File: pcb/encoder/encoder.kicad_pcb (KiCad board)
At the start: 2 copper layers, 23.7 x 15.3 mm, 18 parts, among them J1 Conn_01x05, Q1 B19H1PT, Q2 B19H1PT, Q3 B19H1PT, Q4 B19H1PT, U1 LM358LV

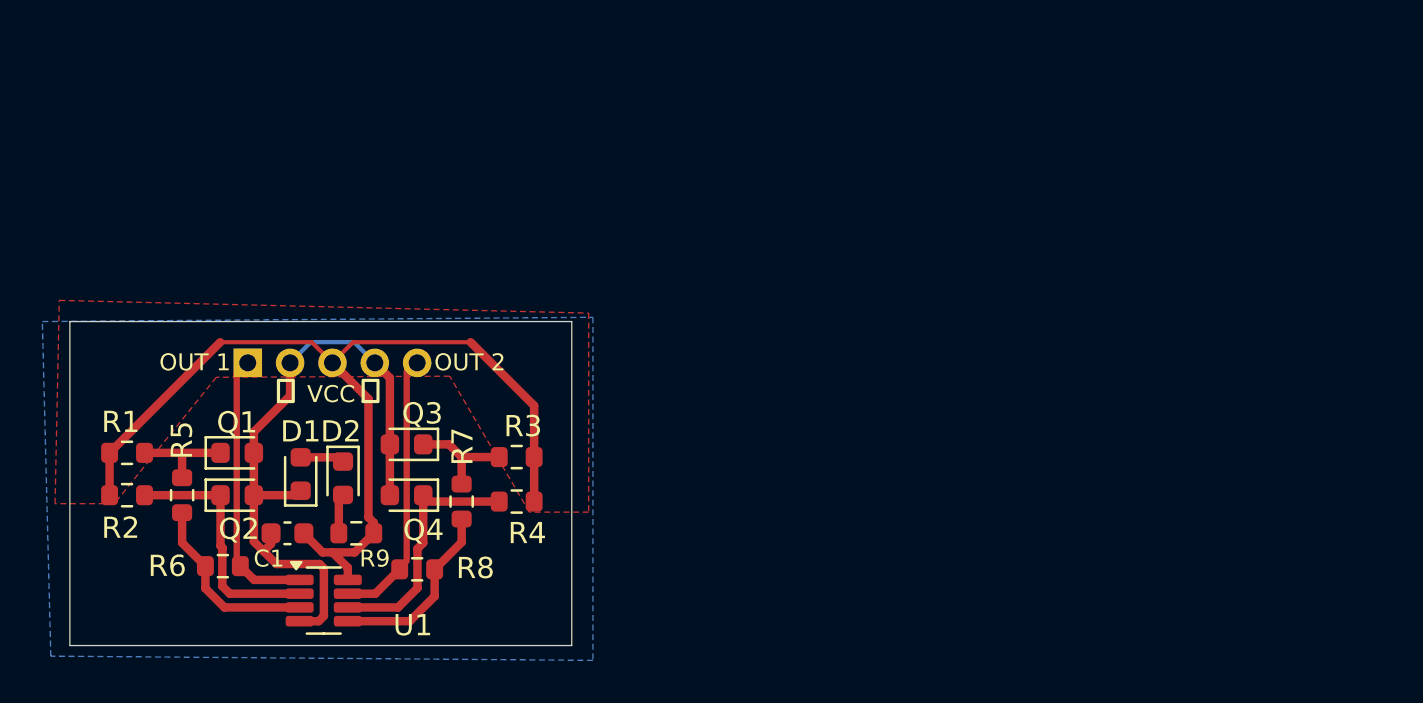
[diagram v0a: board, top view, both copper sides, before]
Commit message: Update to separate pick-up and illumination.
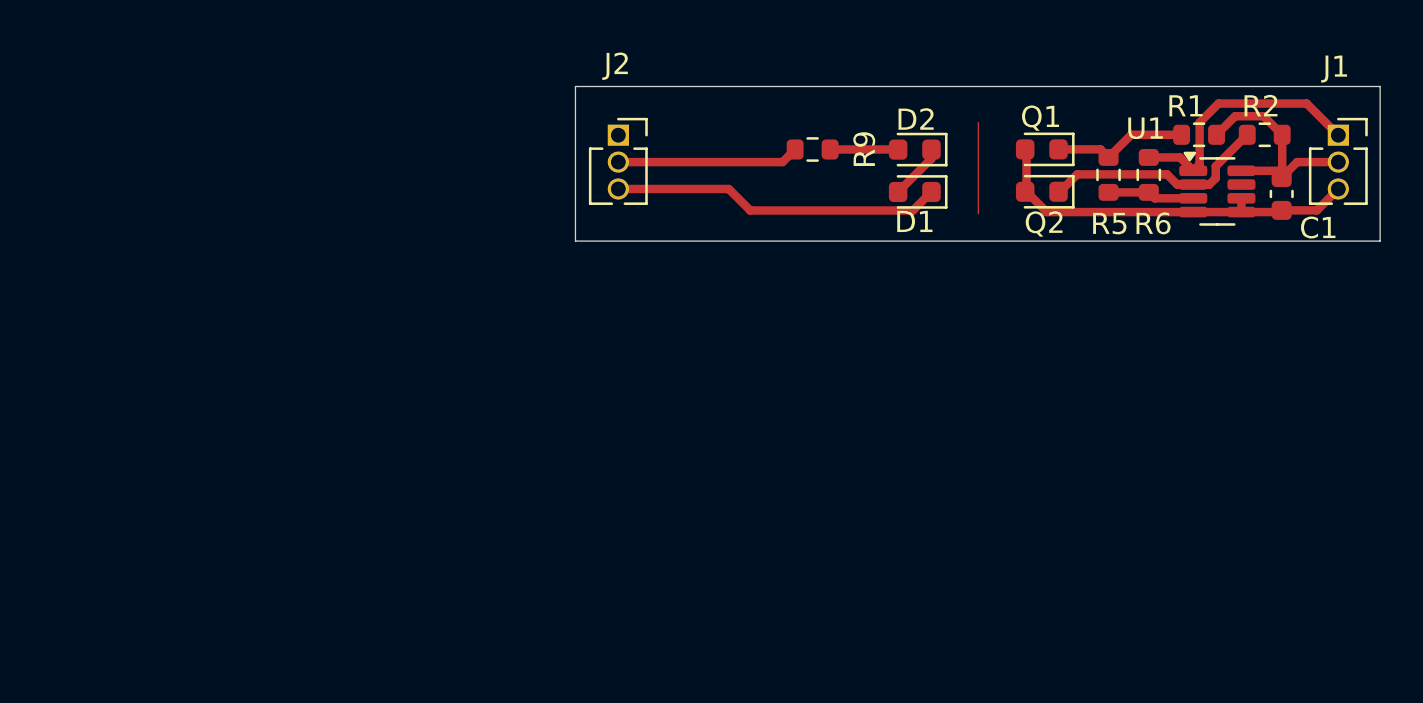
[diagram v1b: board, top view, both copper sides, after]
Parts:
- removed Q3, Q4: B19H1PT, LED_SMD:LED_0603_1608Metric
- removed R3, R4, R7, R8: R, Resistor_SMD:R_0603_1608Metric
- added J2: Conn_01x03_Pin, Connector_PinSocket_1.27mm:PinSocket_1x03_P1.27mm_Vertical, F.Cu at (58.0, 35.0)
- J1: value Conn_01x05 -> Conn_01x03_Pin; footprint Connector_PinHeader_2.00mm:PinHeader_1x05_P2.00mm_Vertical -> Connector_PinSocket_1.27mm:PinSocket_1x03_P1.27mm_Vertical
- moved R2 56.4 mm to (88.5, 35.0), turned to 180 degrees
- moved R1 52.8 mm to (85.4, 35.0), turned to 180 degrees
- moved J1 52.6 mm to (92.0, 35.0), turned to 0 degrees
- moved C1 49.6 mm to (89.3, 37.8), turned to -90 degrees
- moved R6 47.5 mm to (83.0, 36.9), turned to 90 degrees
- moved U1 46.4 mm to (86.3, 37.7)
- moved R5 46.3 mm to (81.2, 36.9)
- moved Q1 40.6 mm to (78.0, 35.7), turned to 180 degrees
- moved Q2 40.6 mm to (78.0, 37.7), turned to 180 degrees
- moved D1 31.9 mm to (72.0, 37.7), turned to 180 degrees
- moved D2 31.1 mm to (72.0, 35.7), turned to 180 degrees
- moved R9 28.2 mm to (67.2, 35.7), turned to 0 degrees
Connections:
- J1 pad 2: GND -> VCC
- J1 pad 3: VCC -> GND
- U1 pad 5: Net-(U1B-+) -> GND
- U1 pad 6: Net-(Q4-C) -> GND
- U1 pad 7: /Out_2 -> unconnected-(U1-Pad7)
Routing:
- net VCC: track 45.4 -> 19.7 mm
- net /Out_2: track 13.0 -> 0.00 mm
- net Net-(Q4-C): track 12.0 -> 0.00 mm
- net Net-(U1B-+): track 8.76 -> 0.00 mm
- net Net-(Q3-C): track 5.11 -> 0.00 mm
- net Net-(U1A-+): track 8.96 -> 4.40 mm
- net GND: track 31.7 -> 34.0 mm
- net Net-(Q1-C): track 4.76 -> 6.49 mm
- net Net-(D2-A): track 2.13 -> 3.29 mm
- net Net-(Q2-C): track 11.7 -> 10.7 mm
- net Net-(D1-A): track 2.08 -> 3.13 mm
- removed copper zone on B.Cu, net GND
- removed copper zone on F.Cu, net VCC
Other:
- board size 23.7 x 15.3 mm -> 38 x 7.3 mm
- board text removed: "OUT 1"
- board text removed: "OUT 2"
- board text removed: "VCC"
- board text removed: "⏚"

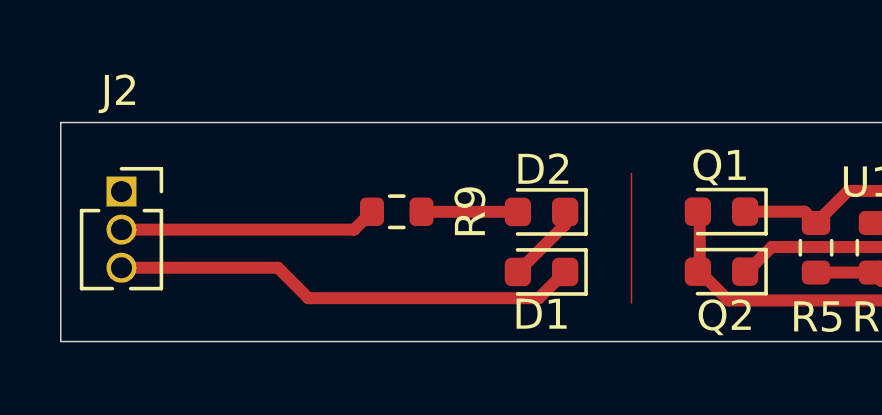
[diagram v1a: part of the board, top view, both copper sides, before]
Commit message: Some README refinements.
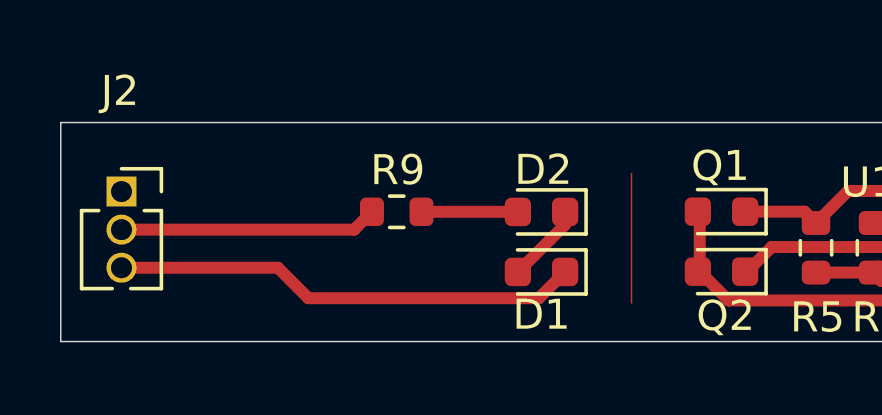
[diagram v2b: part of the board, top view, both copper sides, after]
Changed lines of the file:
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@@
 		(tags "Through hole socket strip THT 1x03 1.27mm single row")
 		(property "Reference" "J2"
-			(at -0.05 -3.35 360)
+			(at -0.05 -3.35 0)
 			(layer "F.SilkS")
 			(effects
@@
 		)
 		(property "Value" "Conn_01x03_Pin"
-			(at 0 4.675 360)
+			(at 0 4.675 0)
 			(layer "F.Fab")
 			(effects
@@
 		)
 		(model "${KICAD8_3DMODEL_DIR}/Connector_PinSocket_1.27mm.3dshapes/PinSocket_1x03_P1.27mm_Vertical.wrl"
+			(hide yes)
 			(offset
 				(xyz 0 0 0)
@@
 		(tags "LED")
 		(property "Reference" "Q2"
-			(at -0.1375 -1.48 360)
+			(at -0.1375 -1.48 0)
 			(layer "F.SilkS")
 			(effects
@@
 		)
 		(property "Value" "B19H1PT"
-			(at 0 1.43 360)
+			(at 0 1.43 0)
 			(layer "F.Fab")
 			(effects
@@
 		)
 		(fp_text user "${REFERENCE}"
-			(at 0 0 360)
+			(at 0 0 0)
 			(layer "F.Fab")
 			(effects
@@
 		(tags "LED")
 		(property "Reference" "D1"
-			(at 0 -1.43 360)
+			(at 0 -1.43 0)
 			(layer "F.SilkS")
 			(effects
@@
 		)
 		(property "Value" "LED"
-			(at 0 1.43 360)
+			(at 0 1.43 0)
 			(layer "F.Fab")
 			(effects
@@
 		)
 		(fp_text user "${REFERENCE}"
-			(at 0 0 360)
+			(at 0 0 0)
 			(layer "F.Fab")
 			(effects
@@
 		(tags "resistor")
 		(property "Reference" "R9"
-			(at 2.475 0 90)
+			(at 0.0334 -1.385 180)
 			(layer "F.SilkS")
 			(effects
@@
 		)
 		(property "Value" "R"
-			(at 0 1.43 360)
+			(at 0 1.43 0)
 			(layer "F.Fab")
 			(effects
@@
 		)
 		(fp_text user "${REFERENCE}"
-			(at 0 0 360)
+			(at 0 0 0)
 			(layer "F.Fab")
 			(effects
@@
 		(tags "Through hole socket strip THT 1x03 1.27mm single row")
 		(property "Reference" "J1"
-			(at -0.1 -3.225 360)
+			(at -0.1 -3.225 0)
 			(layer "F.SilkS")
 			(effects
@@
 		)
 		(property "Value" "Conn_01x03_Pin"
-			(at 0 4.675 360)
+			(at 0 4.675 0)
 			(layer "F.Fab")
 			(effects
@@
 		)
 		(model "${KICAD8_3DMODEL_DIR}/Connector_PinSocket_1.27mm.3dshapes/PinSocket_1x03_P1.27mm_Vertical.wrl"
+			(hide yes)
 			(offset
 				(xyz 0 0 0)
@@
 		(tags "resistor")
 		(property "Reference" "R1"
-			(at 0.625 1.33 360)
+			(at 0.625 1.33 0)
 			(layer "F.SilkS")
 			(effects
@@
 		)
 		(property "Value" "R"
-			(at 0 1.43 360)
+			(at 0 1.43 0)
 			(layer "F.Fab")
 			(effects
@@
 		)
 		(fp_text user "${REFERENCE}"
-			(at 0 0 360)
+			(at 0 0 0)
 			(layer "F.Fab")
 			(effects
@@
 		(tags "LED")
 		(property "Reference" "D2"
-			(at -0.0625 1.4 360)
+			(at -0.0625 1.4 0)
 			(layer "F.SilkS")
 			(effects
@@
 		)
 		(property "Value" "LED"
-			(at 0 1.43 360)
+			(at 0 1.43 0)
 			(layer "F.Fab")
 			(effects
@@
 		)
 		(fp_text user "${REFERENCE}"
-			(at 0 0 360)
+			(at 0 0 0)
 			(layer "F.Fab")
 			(effects
@@
 		(tags "LED")
 		(property "Reference" "Q1"
-			(at 0.0375 1.52 360)
+			(at 0.0375 1.52 0)
 			(layer "F.SilkS")
 			(effects
@@
 		)
 		(property "Value" "B19H1PT"
-			(at 0 1.43 360)
+			(at 0 1.43 0)
 			(layer "F.Fab")
 			(effects
@@
 		)
 		(fp_text user "${REFERENCE}"
-			(at 0 0 360)
+			(at 0 0 0)
 			(layer "F.Fab")
 			(effects
@@
 		(tags "resistor")
 		(property "Reference" "R2"
-			(at 0.175 1.33 360)
+			(at 0.175 1.33 0)
 			(layer "F.SilkS")
 			(effects
@@
 		)
 		(property "Value" "R"
-			(at 0 1.43 360)
+			(at 0 1.43 0)
 			(layer "F.Fab")
 			(effects
@@
 		)
 		(fp_text user "${REFERENCE}"
-			(at 0 0 360)
-			(layer "F.Fab")
-			(effects
+			(at 0 0 0)
+			(layer "F.Fab")
+			(effects
